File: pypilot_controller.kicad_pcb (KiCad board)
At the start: 4 copper layers, 76.6 x 50.6 mm, 82 parts, among them J1 power+, J2 power-, J3 power+, J4 power+, J5 UART_Device, J6 Rudder, J7 End Stops, J8 Conn_01x02, J9 ISP, Q1 Q_NMOS_GDS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

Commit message: Switch footprints to stock KiCad versions, if the stock one is equivalent
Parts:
- C10, C9: footprint pypilot_footprints:CP_Radial_D10.0mm_P5.00mm -> Capacitor_THT:CP_Radial_D10.0mm_P5.00mm
- D1, D2: footprint wp_footprints:DO-214AC -> Diode_SMD:D_SMA
- J9: footprint pypilot_footprints:PinHeader_2x03_P2.54mm_Vertical_SMD -> Connector_PinHeader_2.54mm:PinHeader_2x03_P2.54mm_Vertical_SMD
- Q1, Q2, Q3, Q4, Q5: footprint pypilot_footprints:TO-252-2_270 -> Package_TO_SOT_SMD:TO-252-2_270
- R20: footprint pypilot_controller_footprints:Resistor_Horizontal_RM10mm -> Resistor_THT:R_Axial_DIN0207_L6.3mm_D2.5mm_P15.24mm_Horizontal
- U1, U5, U8: footprint pypilot_footprints:SOT-23-5 -> Package_TO_SOT_SMD:SOT-23-5
- U10, U9: footprint pypilot_footprints:SO-5_4.4x3.6mm_P1.27mm -> Package_SO:SO-5_4.4x3.6mm_P1.27mm
- U2, U3: footprint pypilot_footprints:SOIC-8_3.9x4.9mm_P1.27mm -> Package_SO:SOIC-8_3.9x4.9mm_P1.27mm
- U4: footprint pypilot_footprints:SOT-223-3_TabPin2_180 -> Package_TO_SOT_SMD:SOT-223-3_TabPin2
- U6: footprint pypilot_footprints:TO-252-2 -> Package_TO_SOT_SMD:TO-252-2
- U7: footprint pypilot_footprints:TQFP-32_7x7mm_P0.8mm -> Package_QFP:TQFP-32_7x7mm_P0.8mm
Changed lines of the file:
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@@
     )
   )
-  (module wp_footprints:DO-214AC (layer F.Cu)
+  (module Diode_SMD:D_SMA (layer F.Cu)
     (at 24.7614 3.911 180)
     (attr smd)
@@
       (net 4 "Net-(C5-Pad1)"))
   )
-  (module wp_footprints:DO-214AC (layer F.Cu)
+  (module Diode_SMD:D_SMA (layer F.Cu)
     (at 38.6842 3.8354 180)
     (attr smd)
@@
       (net 57 "Net-(C1-Pad2)"))
   )
-  (module pypilot_controller_footprints:Resistor_Horizontal_RM10mm (layer F.Cu)
+  (module Resistor_THT:R_Axial_DIN0207_L6.3mm_D2.5mm_P15.24mm_Horizontal (layer F.Cu)
     (at 43.9366 29.0322 180)
     (descr "Resistor, Axial,  RM 10mm, 1/3W")
@@
     )
   )
-  (module pypilot_footprints:SOT-23-5 (layer F.Cu)
+  (module Package_TO_SOT_SMD:SOT-23-5 (layer F.Cu)
     (at 61.1886 43.2394 90)
     (descr "5-pin SOT23 package")
@@
     )
   )
-  (module pypilot_footprints:SOT-23-5 (layer F.Cu)
+  (module Package_TO_SOT_SMD:SOT-23-5 (layer F.Cu)
     (at 71.2724 43.8658)
     (descr "5-pin SOT23 package")
@@
     )
   )
-  (module pypilot_footprints:SOT-23-5 (layer F.Cu)
+  (module Package_TO_SOT_SMD:SOT-23-5 (layer F.Cu)
     (at 67.0814 41.2242 270)
     (descr "5-pin SOT23 package")
@@
     )
   )
-  (module pypilot_footprints:SO-5_4.4x3.6mm_P1.27mm (layer F.Cu)
+  (module Package_SO:SO-5_4.4x3.6mm_P1.27mm (layer F.Cu)
     (at 59.309 34.6706 90)
     (descr "5-Lead Plastic Small Outline (SO), see https://docs.broadcom.com/cs/Satellite?blobcol=urldata&blobheader=application%2Fpdf&blobheadername1=Content-Disposition&blobheadername2=Content-Type&blobheadername3=MDT-Type&blobheadervalue1=attachment%3Bfilename%3DIPD-Selection-Guide_AV00-0254EN_030617.pdf&blobheadervalue2=application%2Fx-download&blobheadervalue3=abinary%253B%2Bcharset%253DUTF-8&blobkey=id&blobnocache=true&blobtable=MungoBlobs&blobwhere=1430884105675&ssbinary=true")
@@
     )
   )
-  (module pypilot_footprints:SO-5_4.4x3.6mm_P1.27mm (layer F.Cu)
+  (module Package_SO:SO-5_4.4x3.6mm_P1.27mm (layer F.Cu)
     (at 63.6524 34.671 270)
     (descr "5-Lead Plastic Small Outline (SO), see https://docs.broadcom.com/cs/Satellite?blobcol=urldata&blobheader=application%2Fpdf&blobheadername1=Content-Disposition&blobheadername2=Content-Type&blobheadername3=MDT-Type&blobheadervalue1=attachment%3Bfilename%3DIPD-Selection-Guide_AV00-0254EN_030617.pdf&blobheadervalue2=application%2Fx-download&blobheadervalue3=abinary%253B%2Bcharset%253DUTF-8&blobkey=id&blobnocache=true&blobtable=MungoBlobs&blobwhere=1430884105675&ssbinary=true")
@@
     )
   )
-  (module pypilot_footprints:CP_Radial_D10.0mm_P5.00mm (layer F.Cu)
+  (module Capacitor_THT:CP_Radial_D10.0mm_P5.00mm (layer F.Cu)
     (at 11.749967 18.374433 45)
     (descr "CP, Radial series, Radial, pin pitch=5.00mm, , diameter=10mm, Electrolytic Capacitor")
@@
     )
   )
-  (module pypilot_footprints:CP_Radial_D10.0mm_P5.00mm (layer F.Cu)
+  (module Capacitor_THT:CP_Radial_D10.0mm_P5.00mm (layer F.Cu)
     (at 22.443367 18.501433 45)
     (descr "CP, Radial series, Radial, pin pitch=5.00mm, , diameter=10mm, Electrolytic Capacitor")
@@
       (net 25 "Net-(C6-Pad2)"))
   )
-  (module pypilot_footprints:PinHeader_2x03_P2.54mm_Vertical_SMD (layer F.Cu)
+  (module Connector_PinHeader_2.54mm:PinHeader_2x03_P2.54mm_Vertical_SMD (layer F.Cu)
     (at 72.0598 29.6164 270)
     (descr "surface-mounted straight pin header, 2x03, 2.54mm pitch, double rows")
@@
     )
   )
-  (module pypilot_footprints:SOIC-8_3.9x4.9mm_P1.27mm (layer F.Cu)
+  (module Package_SO:SOIC-8_3.9x4.9mm_P1.27mm (layer F.Cu)
     (at 25.1864 8.266 270)
     (descr "SOIC, 8 Pin (JEDEC MS-012AA, https://www.analog.com/media/en/package-pcb-resources/package/pkg_pdf/soic_narrow-r/r_8.pdf), generated with kicad-footprint-generator ipc_gullwing_generator.py")
@@
     )
   )
-  (module pypilot_footprints:SOIC-8_3.9x4.9mm_P1.27mm (layer F.Cu)
+  (module Package_SO:SOIC-8_3.9x4.9mm_P1.27mm (layer F.Cu)
     (at 36.3412 8.2406 270)
     (descr "SOIC, 8 Pin (JEDEC MS-012AA, https://www.analog.com/media/en/package-pcb-resources/package/pkg_pdf/soic_narrow-r/r_8.pdf), generated with kicad-footprint-generator ipc_gullwing_generator.py")
@@
     )
   )
-  (module pypilot_footprints:SOT-223-3_TabPin2_180 (layer F.Cu)
+  (module Package_TO_SOT_SMD:SOT-223-3_TabPin2 (layer F.Cu)
     (at 60.579 6.0452)
     (descr "module CMS SOT223 4 pins")
@@
     )
   )
-  (module pypilot_footprints:TQFP-32_7x7mm_P0.8mm (layer F.Cu)
+  (module Package_QFP:TQFP-32_7x7mm_P0.8mm (layer F.Cu)
     (at 60.0456 18.034 90)
     (descr "32-Lead Plastic Thin Quad Flatpack (PT) - 7x7x1.0 mm Body, 2.00 mm [TQFP] (see Microchip Packaging Specification 00000049BS.pdf)")
@@
       (net 24 "Net-(C5-Pad2)"))
   )
-  (module pypilot_footprints:TO-252-2 (layer F.Cu)
+  (module Package_TO_SOT_SMD:TO-252-2 (layer F.Cu)
     (at 12.1158 9.398)
     (descr "TO-252 / DPAK SMD package, http://www.infineon.com/cms/en/product/packages/PG-TO252/PG-TO252-3-1/")
@@
     )
   )
-  (module pypilot_footprints:TO-252-2_270 (layer F.Cu)
+  (module Package_TO_SOT_SMD:TO-252-2_270 (layer F.Cu)
     (at 45.9232 31.8516 90)
     (descr "TO-252 / DPAK SMD package, http://www.infineon.com/cms/en/product/packages/PG-TO252/PG-TO252-3-1/")
@@
     )
   )
-  (module pypilot_footprints:TO-252-2_270 (layer F.Cu)
+  (module Package_TO_SOT_SMD:TO-252-2_270 (layer F.Cu)
     (at 35.1106 34.4922 270)
     (descr "TO-252 / DPAK SMD package, http://www.infineon.com/cms/en/product/packages/PG-TO252/PG-TO252-3-1/")
@@
     )
   )
-  (module pypilot_footprints:TO-252-2_270 (layer F.Cu)
+  (module Package_TO_SOT_SMD:TO-252-2_270 (layer F.Cu)
     (at 21.7248 34.4414 270)
     (descr "TO-252 / DPAK SMD package, http://www.infineon.com/cms/en/product/packages/PG-TO252/PG-TO252-3-1/")
@@
     )
   )
-  (module pypilot_footprints:TO-252-2_270 (layer F.Cu)
+  (module Package_TO_SOT_SMD:TO-252-2_270 (layer F.Cu)
     (at 44.5018 23.023 180)
     (descr "TO-252 / DPAK SMD package, http://www.infineon.com/cms/en/product/packages/PG-TO252/PG-TO252-3-1/")
@@
     )
   )
-  (module pypilot_footprints:TO-252-2_270 (layer F.Cu)
+  (module Package_TO_SOT_SMD:TO-252-2_270 (layer F.Cu)
     (at 32.1818 25.6032 180)
     (descr "TO-252 / DPAK SMD package, http://www.infineon.com/cms/en/product/packages/PG-TO252/PG-TO252-3-1/")

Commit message: Move footprints into pypilot_controller_footprints, creating from PCB file if missing.
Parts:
- F1: footprint wp_footprints:BladeFuse-CarType -> pypilot_controller_footprints:BladeFuse-CarType
- J1, J2, J3, J4: footprint pypilot_footprints:screw_terminal -> pypilot_controller_footprints:screw_terminal
- TVS1: footprint wp_footprints:DO-214AA -> pypilot_controller_footprints:D_SMB_TVS
- TVS2: footprint pypilot_footprints:DO-214AA -> pypilot_controller_footprints:D_SMB_TVS
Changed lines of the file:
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@@
     )
   )
-  (module wp_footprints:BladeFuse-CarType (layer F.Cu)
+  (module pypilot_controller_footprints:BladeFuse-CarType (layer F.Cu)
     (at 6.15 34.44 90)
     (attr smd)
@@
     )
   )
-  (module wp_footprints:DO-214AA (layer F.Cu)
+  (module pypilot_controller_footprints:D_SMB_TVS (layer F.Cu)
     (at 44.05 37.475 180)
     (descr "DO214AC PACKAGE. MONODIRECTIONAL.")
@@
     )
   )
-  (module pypilot_footprints:screw_terminal (layer F.Cu)
+  (module pypilot_controller_footprints:screw_terminal (layer F.Cu)
     (at 13.9446 44.9834 270)
     (attr smd)
@@
       (net 37 "Net-(F1-Pad1)"))
   )
-  (module pypilot_footprints:screw_terminal (layer F.Cu)
+  (module pypilot_controller_footprints:screw_terminal (layer F.Cu)
     (at 24.4202 45.1306 270)
     (attr smd)
@@
       (net 38 "Net-(J2-Pad1)"))
   )
-  (module pypilot_footprints:screw_terminal (layer F.Cu)
+  (module pypilot_controller_footprints:screw_terminal (layer F.Cu)
     (at 47.7374 45.0648 270)
     (attr smd)
@@
     )
   )
-  (module pypilot_footprints:screw_terminal (layer F.Cu)
+  (module pypilot_controller_footprints:screw_terminal (layer F.Cu)
     (at 37.1494 45.029 270)
     (attr smd)
@@
     )
   )
-  (module pypilot_footprints:DO-214AA (layer F.Cu)
+  (module pypilot_controller_footprints:D_SMB_TVS (layer F.Cu)
     (at 11.85 31.48926 90)
     (descr "DO214AC PACKAGE. MONODIRECTIONAL.")

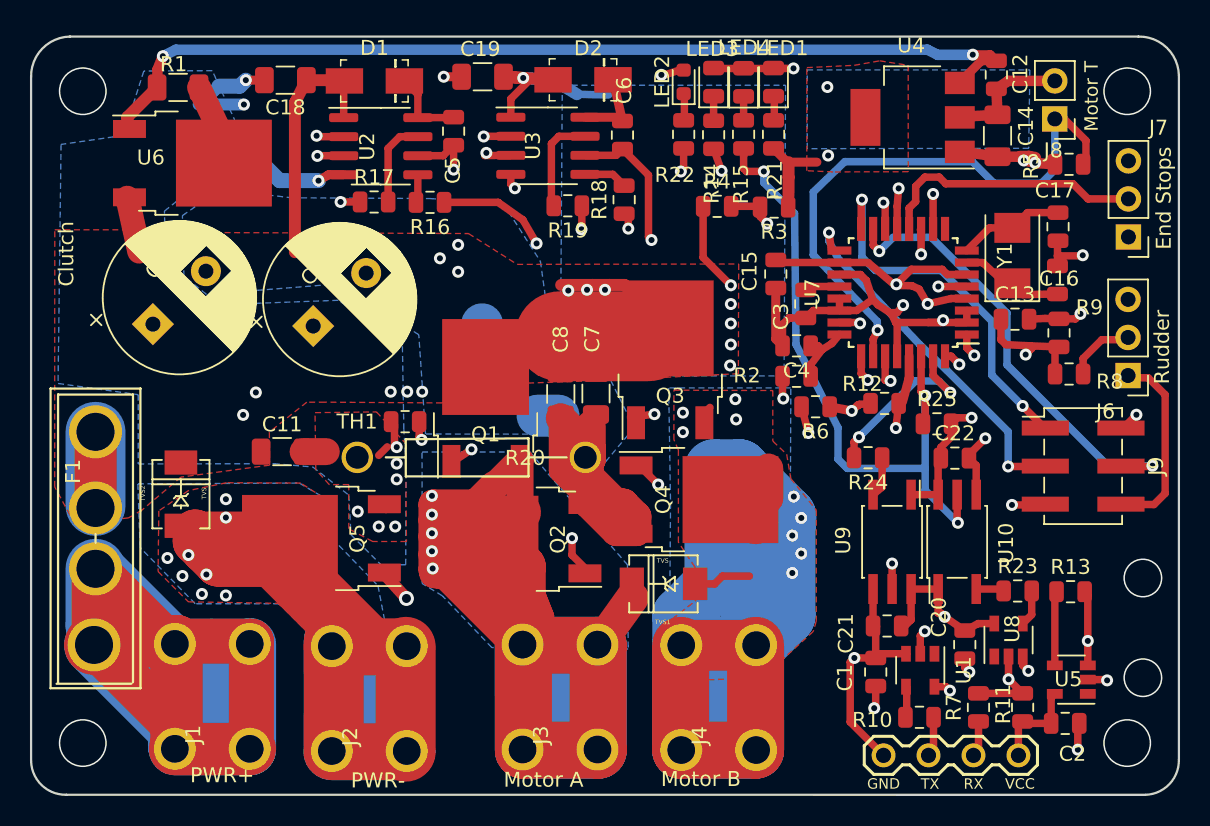
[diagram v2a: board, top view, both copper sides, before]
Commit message: First save of PCB with KiCad 8
Gerbers are equivalent to originals
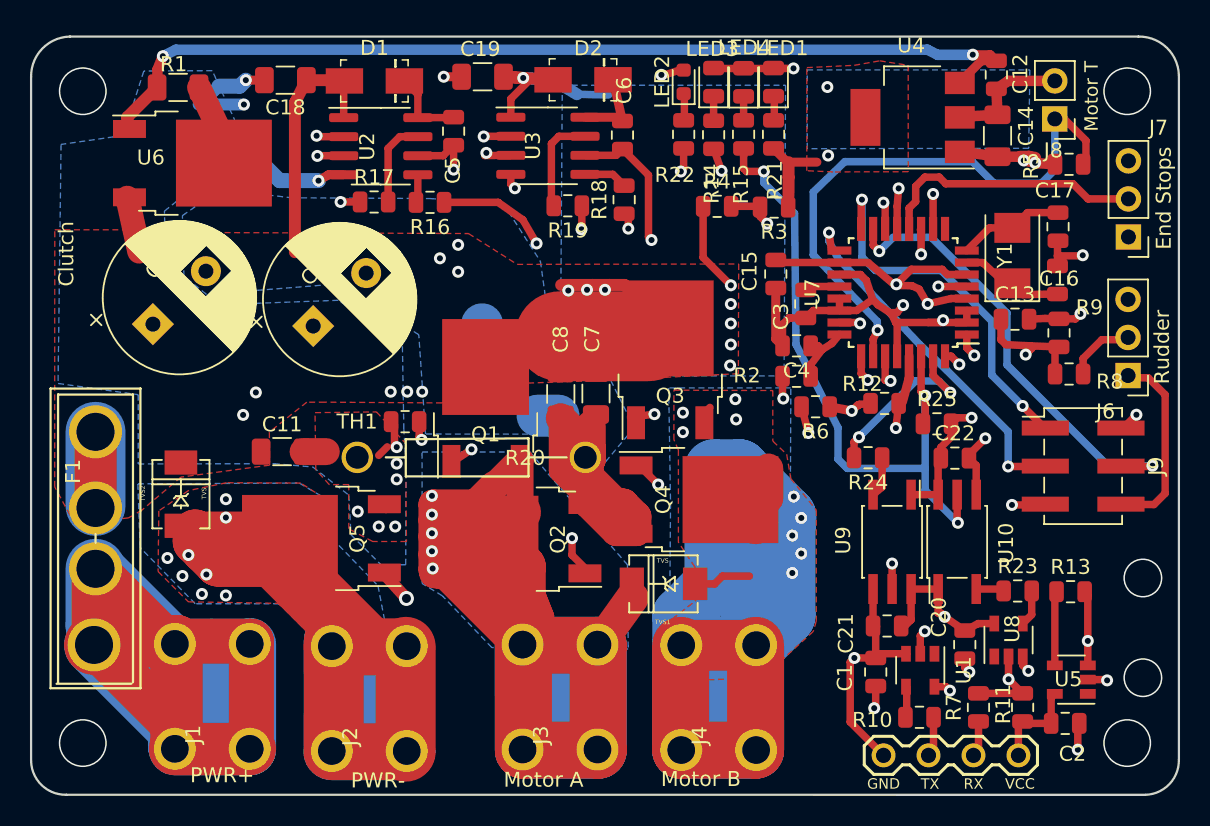
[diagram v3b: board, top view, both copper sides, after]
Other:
- outline, holes or cut-outs redrawn
- net class Default removed

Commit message: Removed fab layers
In this day and age of PnP machines, it's just noise.
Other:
- rule pad_to_mask_clearance: 0.2 -> 0
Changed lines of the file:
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@@
 		(46 "B.CrtYd" user "B.Courtyard")
 		(47 "F.CrtYd" user "F.Courtyard")
-		(48 "B.Fab" user)
-		(49 "F.Fab" user)
 	)
 	(setup
-		(pad_to_mask_clearance 0.2)
-		(solder_mask_min_width 0.25)
+		(pad_to_mask_clearance 0)
 		(allow_soldermask_bridges_in_footprints no)
 		(pcbplotparams

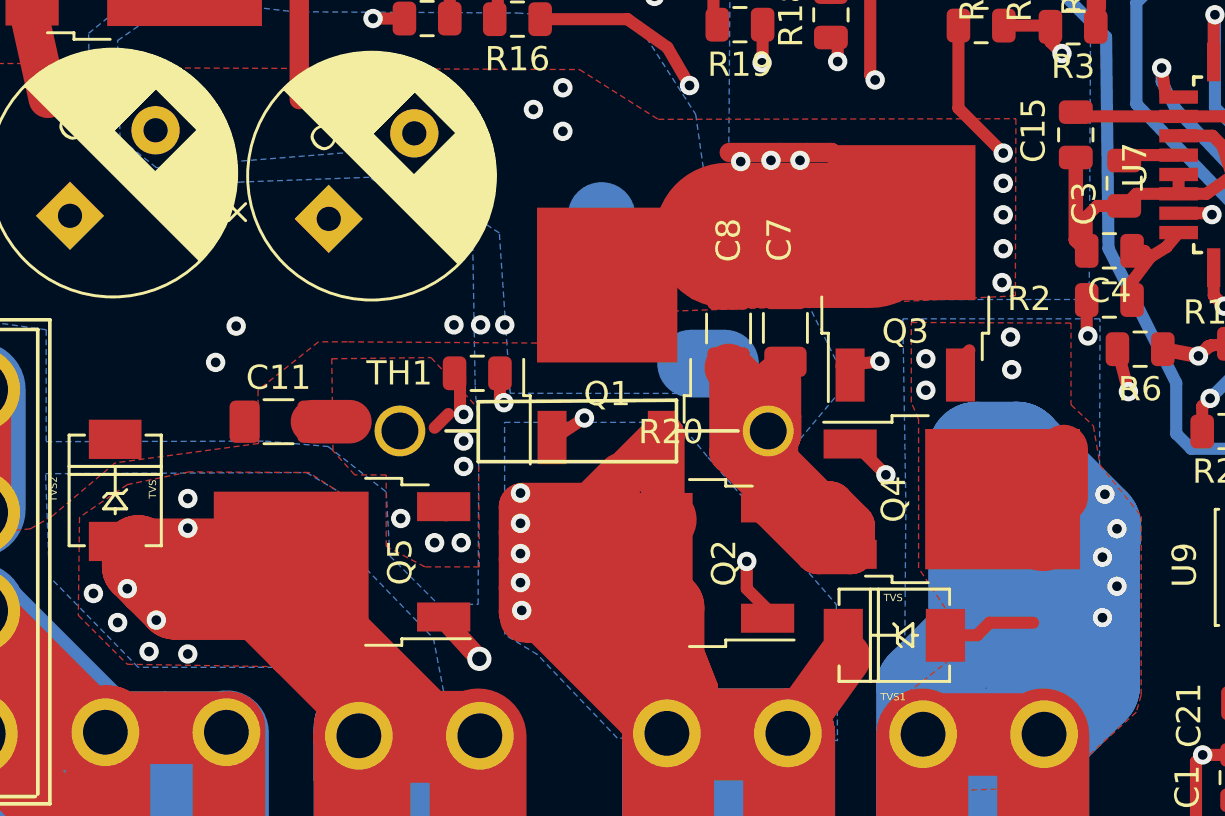
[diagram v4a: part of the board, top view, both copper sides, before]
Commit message: First pull of new footprints and net info from schematic to PCB
It's obviously broken, many footprints aren't oriented or placed
correctly
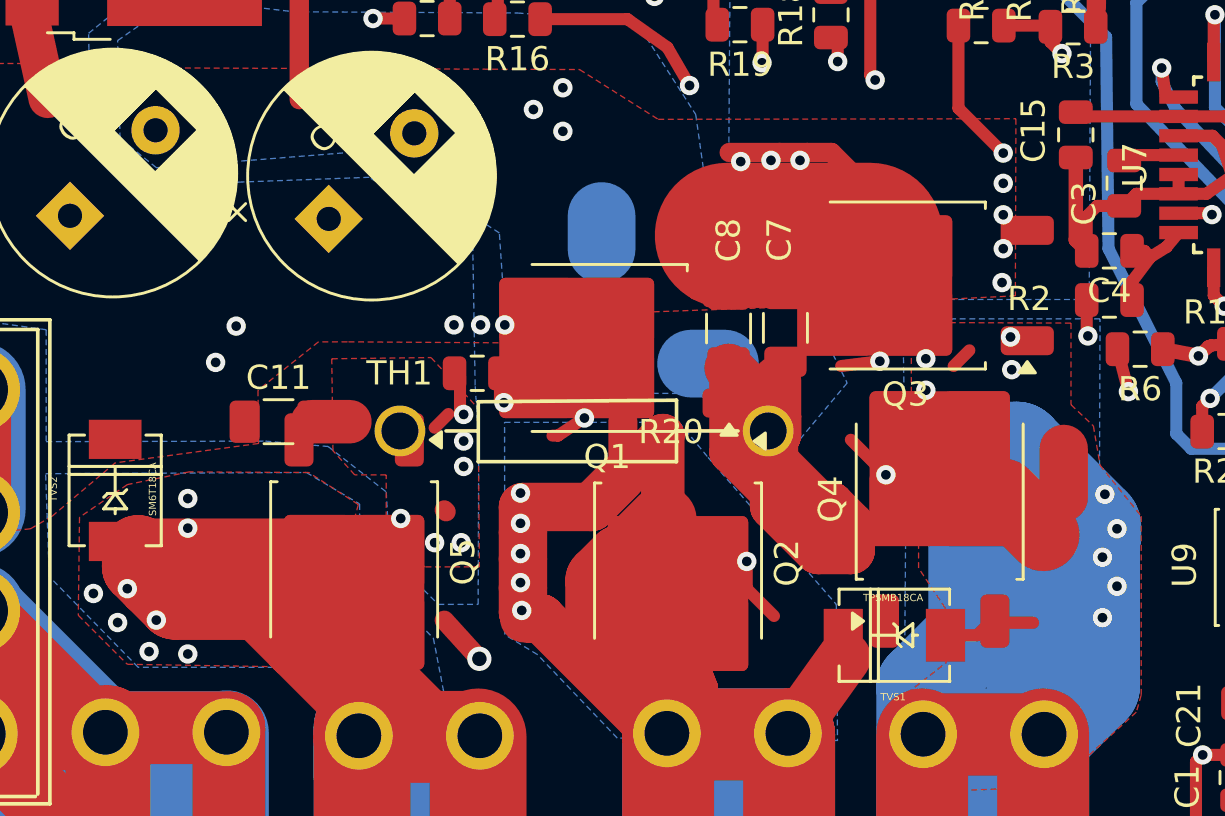
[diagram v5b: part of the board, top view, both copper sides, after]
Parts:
- Q1, Q2, Q3, Q4, Q5: footprint Package_TO_SOT_SMD:TO-252-2_270 -> Package_TO_SOT_SMD:TO-252-2
- TVS1: value TVS -> TPSMB18CA
- TVS2: value TVS -> SM6T18CA
- U7: value ATmega328-AU -> ATmega328P-AU
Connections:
- U7 pad 9: Net-(U7-Pad9) -> unconnected-(U7-PD5-Pad9)
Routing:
- net Net-(J3-Pin_1): track 162.2 -> 0.00 mm, vias 6 -> 0
- net Net-(C5-Pad2): track 0.00 -> 162.2 mm, vias 0 -> 6
- net Net-(C6-Pad2): track 0.00 -> 31.0 mm, vias 0 -> 4
- net Net-(J4-Pin_1): track 134.3 -> 103.3 mm, vias 10 -> 7
- net Net-(Q2-Pad1): track 0.00 -> 30.8 mm, vias 0 -> 2
- net Net-(Q2-G): track 30.8 -> 0.00 mm, vias 2 -> 0
- net Net-(Q4-Pad1): track 0.00 -> 27.7 mm, vias 0 -> 2
- net Net-(Q4-G): track 27.7 -> 0.00 mm, vias 2 -> 0
- net Net-(Q1-Pad1): track 0.00 -> 27.3 mm, vias 0 -> 2
- net Net-(Q1-G): track 27.3 -> 0.00 mm, vias 2 -> 0
- net Net-(Q3-Pad1): track 0.00 -> 18.2 mm, vias 0 -> 2
- net Net-(Q3-G): track 18.2 -> 0.00 mm, vias 2 -> 1
- net Net-(J2-Pin_1): vias 8 -> 9
- net GND: vias 21 -> 20
- net +12V: vias 18 -> 16

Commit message: Rename old nets from KiCad 5 PCB to match net names coming from schematic in KiCad 8
KiCad has changed its algorithm for naming nets.
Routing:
- net Net-(J3-Pin_1): track 0.00 -> 162.2 mm, vias 0 -> 6
- net Net-(C5-Pad2): track 162.2 -> 0.00 mm, vias 6 -> 0
- net Net-(C6-Pad2): track 31.0 -> 0.00 mm, vias 4 -> 0
- net Net-(J4-Pin_1): track 103.3 -> 134.3 mm, vias 7 -> 11
- net Net-(Q2-Pad1): track 30.8 -> 0.00 mm, vias 2 -> 0
- net Net-(Q2-G): track 0.00 -> 30.8 mm, vias 0 -> 2
- net Net-(Q4-Pad1): track 27.7 -> 0.00 mm, vias 2 -> 0
- net Net-(Q4-G): track 0.00 -> 27.7 mm, vias 0 -> 2
- net Net-(Q1-Pad1): track 27.3 -> 0.00 mm, vias 2 -> 0
- net Net-(Q1-G): track 0.00 -> 27.3 mm, vias 0 -> 2
- net Net-(Q3-Pad1): track 18.2 -> 0.00 mm, vias 2 -> 0
- net Net-(Q3-G): track 0.00 -> 18.2 mm, vias 1 -> 3
